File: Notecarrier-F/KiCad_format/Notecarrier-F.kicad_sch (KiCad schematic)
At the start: 15 parts

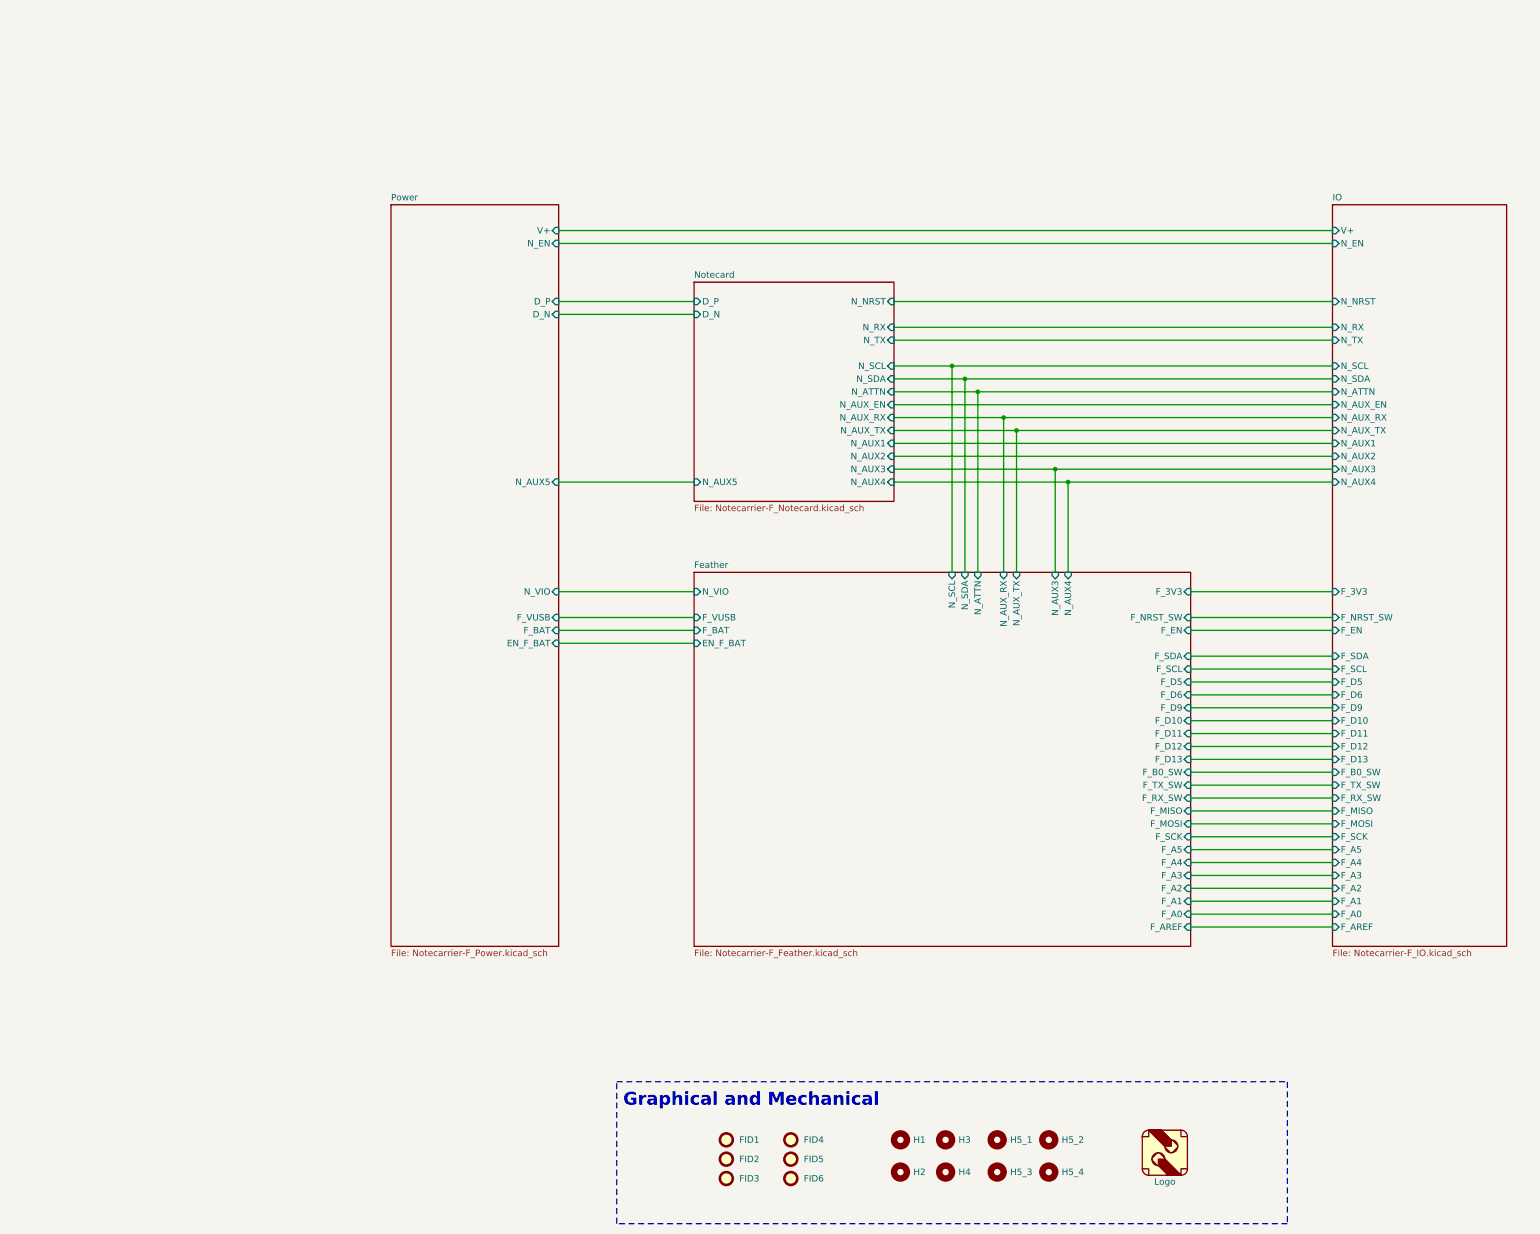
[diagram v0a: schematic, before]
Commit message: Start rev B of Notecarrier-F port
Incorporates changes from Altium design files rev 10 (PCB version 1.2).
Block diagram and schematic first pass complete.
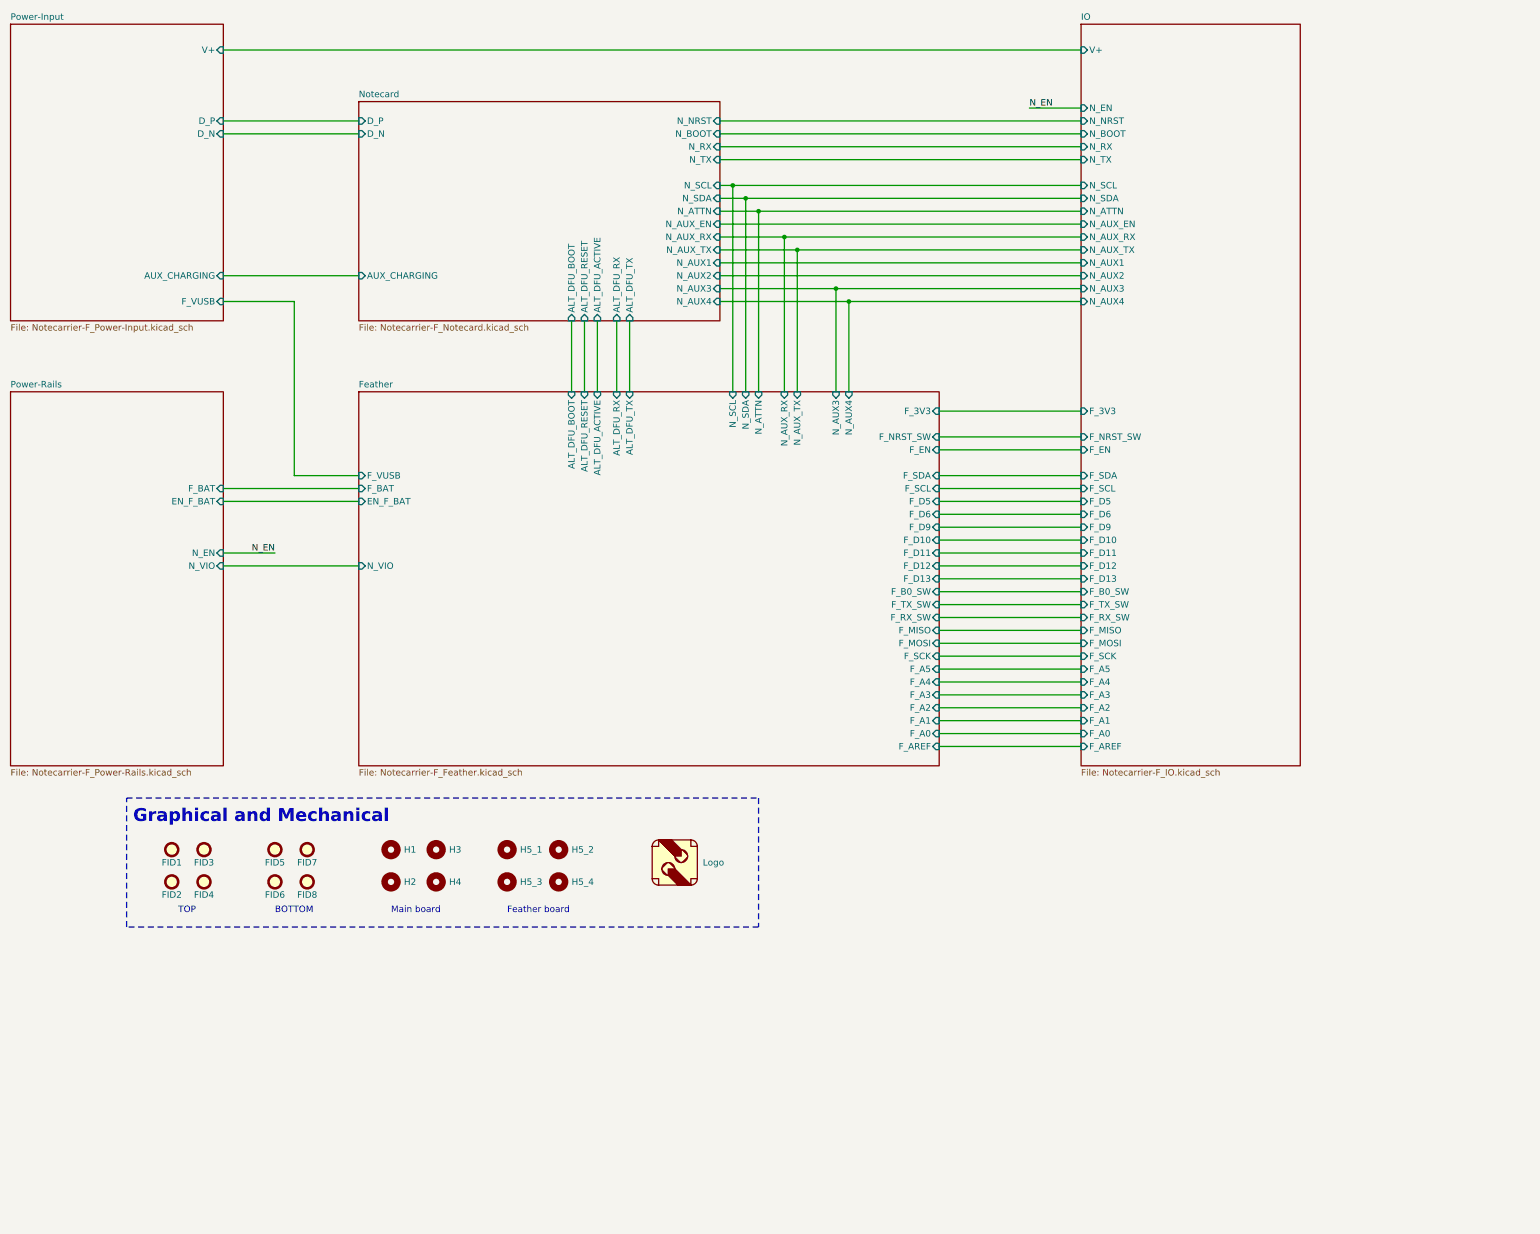
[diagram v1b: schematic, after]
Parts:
- added FID7, FID8: TPS, blues-kicad-lib:FIDUCIAL-F, symbol Mechanical:Fiducial
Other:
- sheet Power renamed Power-Rails
- added sheet Power-Input (Notecarrier-F_Power-Input.kicad_sch)
- sheet Feather ports: added ALT_DFU_ACTIVE, ALT_DFU_BOOT, ALT_DFU_RESET, ALT_DFU_RX, ALT_DFU_TX; removed none
- sheet IO ports: added N_BOOT; removed none
- sheet Notecard ports: added ALT_DFU_ACTIVE, ALT_DFU_BOOT, ALT_DFU_RESET, ALT_DFU_RX, ALT_DFU_TX, AUX_CHARGING, N_BOOT; removed N_AUX5
- sheet Power-Rails: file Notecarrier-F_Power.kicad_sch -> Notecarrier-F_Power-Rails.kicad_sch
- sheet Power-Rails ports: added none; removed D_N, D_P, F_VUSB, N_AUX5, V+
- note added: "BOTTOM"
- note added: "Feather board"
- note added: "Main board"
- note added: "TOP"
- moved on the sheet: FID1, FID2, FID3, FID4, H1, H2, H3, H4, H5_1, H5_2, H5_3, H5_4

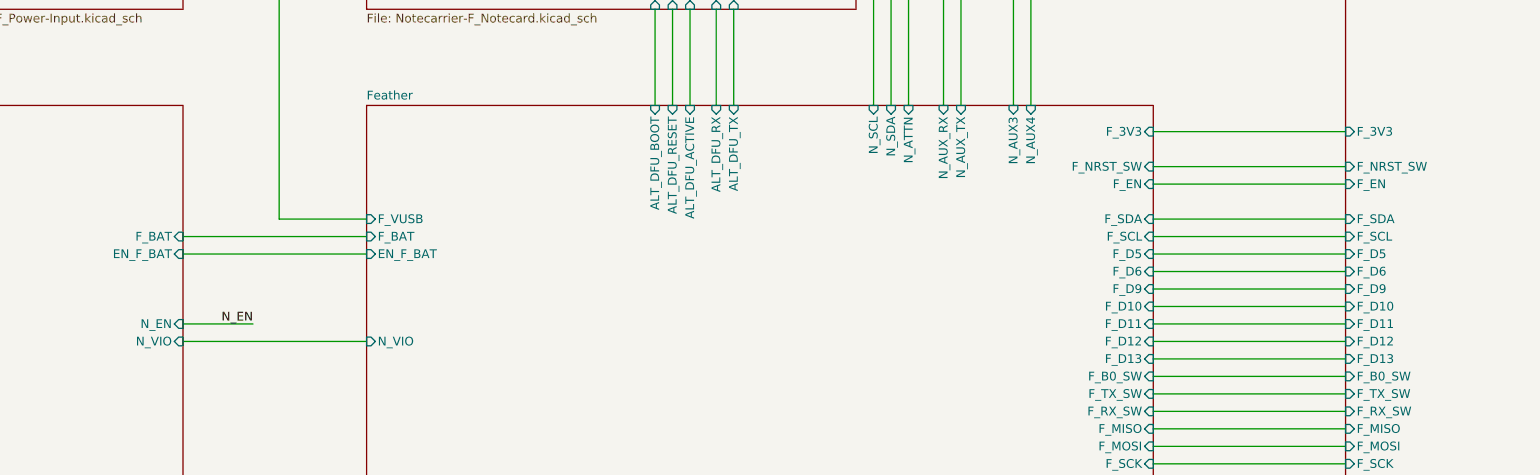
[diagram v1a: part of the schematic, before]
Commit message: Complete first pass PCB rev B.
See README for details. Ready to start Validation.
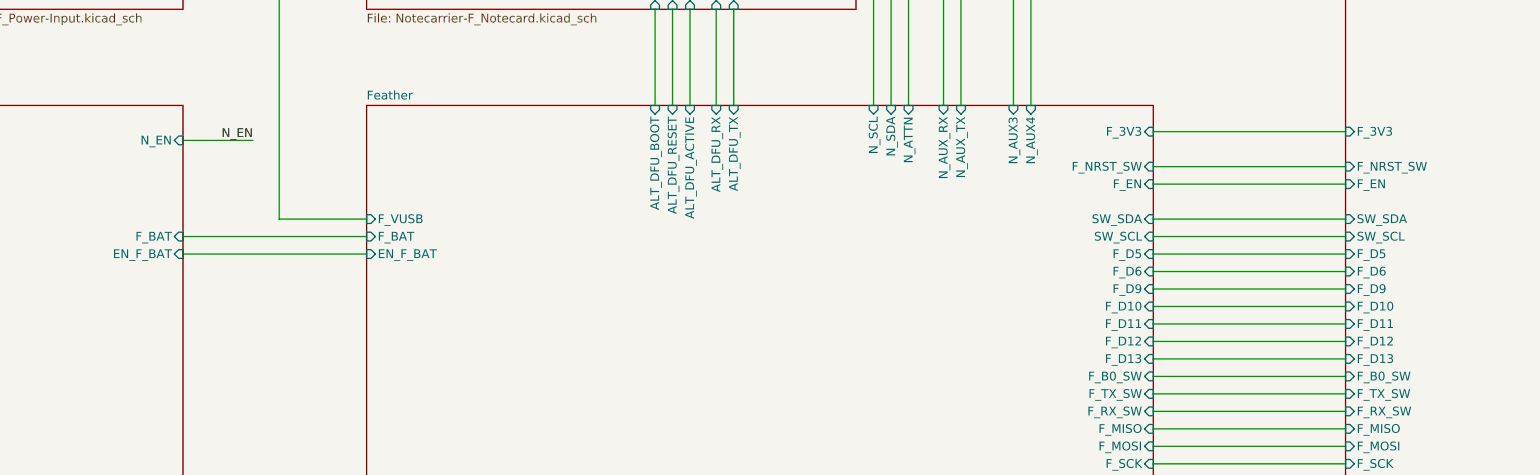
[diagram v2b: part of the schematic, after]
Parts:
- FID1, FID2, FID3, FID4, FID5, FID6, FID7, FID8: footprint blues-kicad-lib:FIDUCIAL-F -> blues-kicad-lib:Fiducial mark 1mm_Fv1.2; now left out of the parts list
- G1: footprint blues-kicad-lib:Logo_19.5x12.5 -> blues-kicad-lib:Logo_23.5x6.1
- H1, H2, H3, H4, H5_1, H5_2, H5_3, H5_4: now left out of the parts list
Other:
- sheet Feather ports: added SW_SCL, SW_SDA; removed F_SCL, F_SDA, N_VIO
- sheet IO ports: added SW_SCL, SW_SDA; removed F_SCL, F_SDA
- sheet Power-Rails ports: added none; removed N_VIO
